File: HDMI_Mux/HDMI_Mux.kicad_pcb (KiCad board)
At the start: 2 copper layers, 12 parts, among them J1 505278-1933, J2 Conn_01x19_MountingPin, J3 Conn_01x19_MountingPin, U1 TS3DV20812, U2 ESD204DQAR-ES, U3 ESD204DQAR-ES, U4 ESD204DQAR-ES, U5 ESD204DQAR-ES

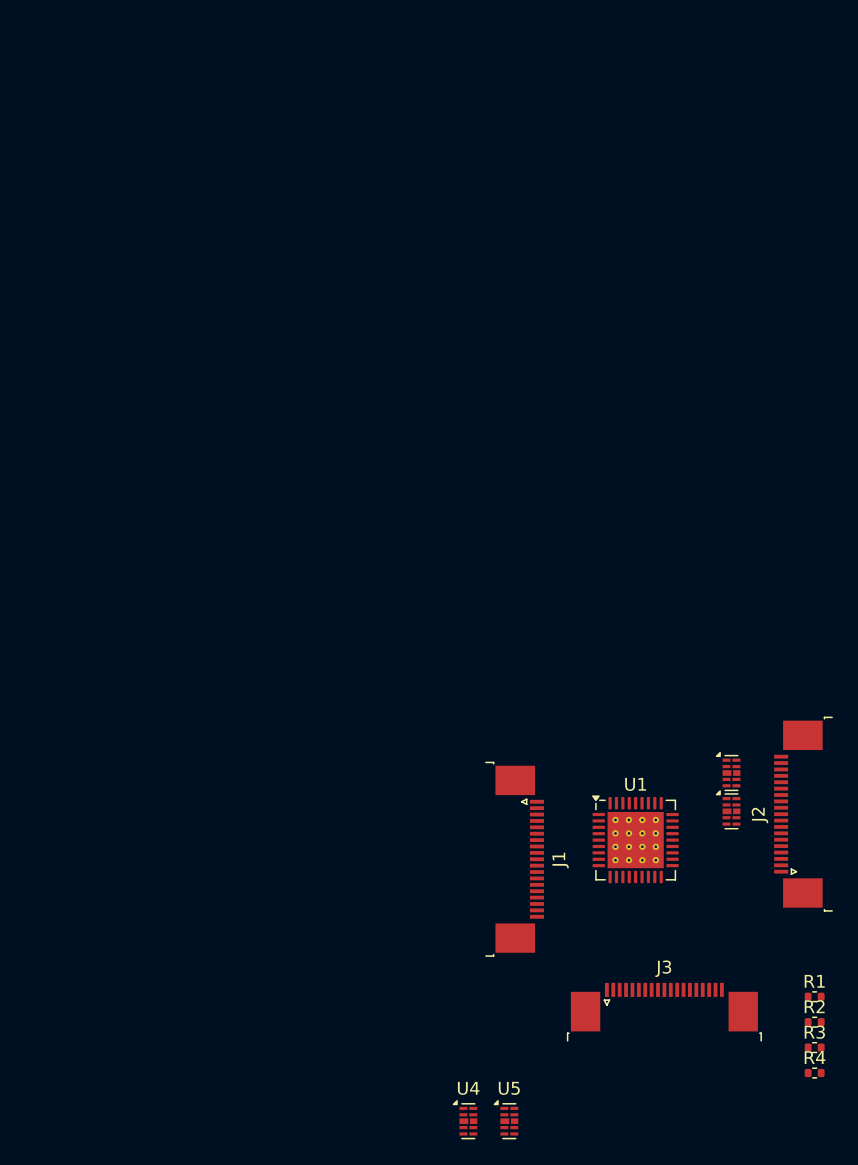
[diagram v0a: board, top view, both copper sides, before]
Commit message: Finish HDMI mux, misc improvements to cafebara
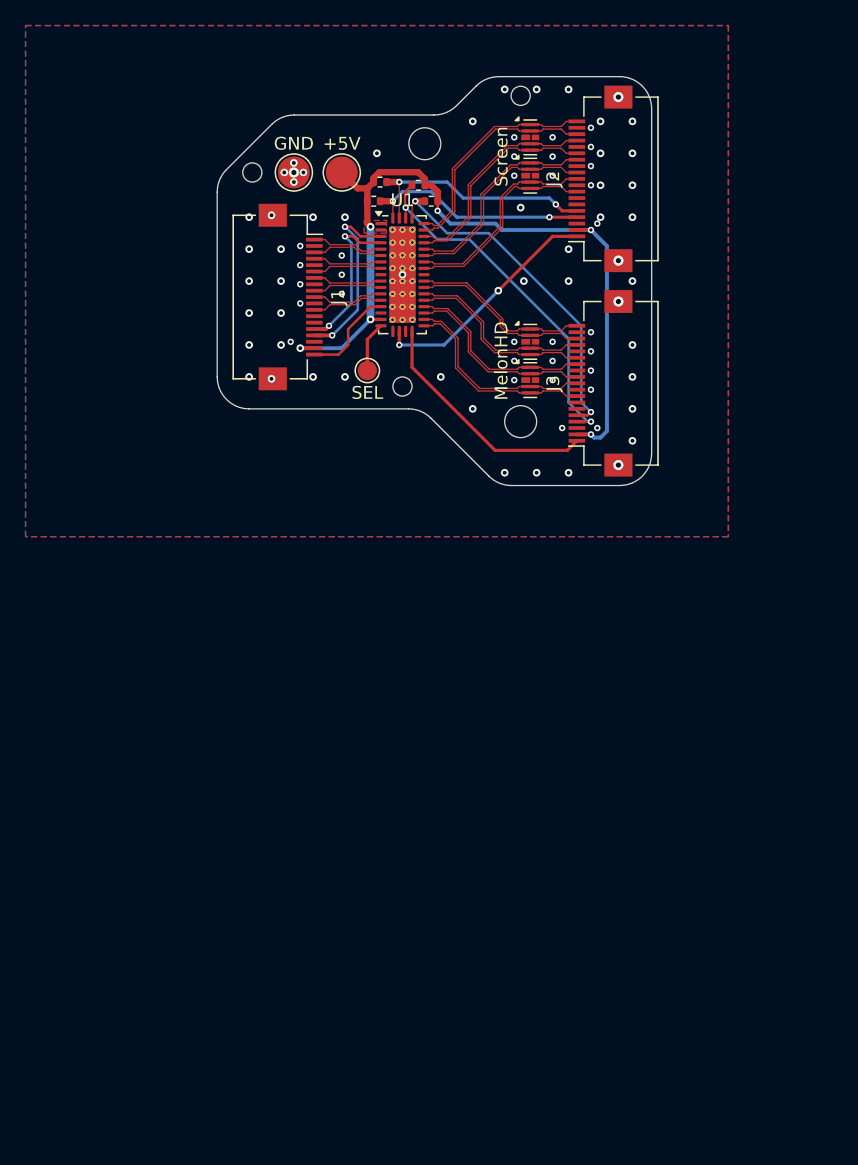
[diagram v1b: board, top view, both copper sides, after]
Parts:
- added TP1: +5V, TestPoint:TestPoint_Pad_D2.5mm, F.Cu at (94.8, 36.5)
- added TP2: GND, TestPoint:TestPoint_Pad_D2.5mm, F.Cu at (91.0, 36.5)
- added TP3: SEL, TestPoint:TestPoint_Pad_D1.5mm, F.Cu at (96.8, 52.0)
- J1, J2, J3: footprint Connector_FFC-FPC:TE_1-1734839-9_1x19-1MP_P0.5mm_Horizontal -> Connector_FFC-FPC:Hirose_FH12-19S-0.5SH_1x19-1MP_P0.50mm_Horizontal
- U1: value TS3DV20812 -> TS3DV642; footprint Package_DFN_QFN:Texas_RHH0036C_VQFN-36-1EP_6x6mm_P0.5mm_EP4.4x4.4mm_ThermalVias -> Package_DFN_QFN:WQFN-42-1EP_3.5x9mm_P0.5mm_EP2.05x7.55mm_ThermalVias
- moved R4 74.5 mm to (101.8, 38.8), turned to 180 degrees
- moved R3 74.3 mm to (100.8, 37.5), turned to 180 degrees
- moved R2 74.0 mm to (97.8, 37.2)
- moved R1 71.2 mm to (97.2, 38.8)
- moved U4 61.2 mm to (109.5, 49.8)
- moved U5 58.0 mm to (109.5, 52.8)
- moved U2 52.2 mm to (109.5, 33.8)
- moved U3 52.2 mm to (109.5, 36.8)
- moved J2 52.1 mm to (115.0, 37.0)
- moved J3 49.1 mm to (115.0, 53.0), turned to 90 degrees
- moved U1 47.9 mm to (99.5, 44.5)
- moved J1 47.5 mm to (90.8, 46.2)
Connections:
- U1 pad 1: TMDS2- -> +5V
- U1 pad 10: TMDSClk- -> TMDS0+
- U1 pad 11: GND -> TMDS0-
- U1 pad 12: /HDMI_SCL -> TMDSClk+
- U1 pad 13: SCL_A -> TMDSClk-
- U1 pad 14: SCL_B -> HPD
- U1 pad 15: TMDSClk_B- -> unconnected-(U1-CEC-Pad15)
- U1 pad 16: TMDSClk_B+ -> +5V
- U1 pad 17: TMDSClk_A- -> /SEL2
- U1 pad 18: TMDSClk_A+ -> unconnected-(U1-CEC_A-Pad18)
- U1 pad 19: TMDS0_B- -> HPD_A
- U1 pad 2: TMDS1+ -> +5V
- U1 pad 20: TMDS0_B+ -> unconnected-(U1-CEC_B-Pad20)
- U1 pad 21: TMDS0_A- -> HPD_B
- U1 pad 22: TMDS0_A+ -> TMDSClk_B-
- U1 pad 23: TMDS1_B- -> TMDSClk_B+
- U1 pad 24: TMDS1_B+ -> TMDS0_B-
- U1 pad 25: TMDS1_A- -> TMDS0_B+
- U1 pad 26: TMDS1_A+ -> TMDS1_B-
- U1 pad 27: SEL -> TMDS1_B+
- U1 pad 3: TMDS1- -> /HDMI_SDA
- U1 pad 30: TMDS2_A- -> unconnected-(U1-NC-Pad30)
- U1 pad 31: TMDS2_A+ -> TMDSClk_A-
- U1 pad 32: HPD_B -> TMDSClk_A+
- U1 pad 33: HPD_A -> TMDS0_A-
- U1 pad 34: HPD -> TMDS0_A+
- U1 pad 35: +3.3V -> TMDS1_A-
- U1 pad 36: TMDS2+ -> TMDS1_A+
- U1 pad 37: GND -> TMDS2_A-
- U1 pad 4: /HDMI_SDA -> /HDMI_SCL
- U1 pad 5: SDA_A -> TMDS2+
- U1 pad 6: SDA_B -> TMDS2-
- U1 pad 7: TMDS0+ -> TMDS1+
- U1 pad 8: TMDS0- -> TMDS1-
- U1 pad 9: TMDSClk+ -> unconnected-(U1-NC-Pad9)
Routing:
- net +5V: track 0.00 -> 62.5 mm, vias 0 -> 6
- net SDA_B: track 0.00 -> 28.3 mm, vias 0 -> 2
- net SCL_B: track 0.00 -> 27.5 mm, vias 0 -> 2
- net HPD_B: track 0.00 -> 18.7 mm
- net SCL_A: track 0.00 -> 18.6 mm, vias 0 -> 2
- net HPD_A: track 0.00 -> 18.5 mm, vias 0 -> 2
- net SDA_A: track 0.00 -> 17.9 mm, vias 0 -> 2
- net TMDS2_A+: track 0.00 -> 17.4 mm
- net TMDS2_A-: track 0.00 -> 17.4 mm
- net TMDS1_A+: track 0.00 -> 16.8 mm
- net TMDS1_A-: track 0.00 -> 16.8 mm
- net TMDS0_A-: track 0.00 -> 16.4 mm
- net TMDS0_A+: track 0.00 -> 16.4 mm
- net TMDSClk_A-: track 0.00 -> 16.2 mm
- net TMDSClk_A+: track 0.00 -> 16.2 mm
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- added copper zone on F.Cu, net +5V
- added copper zone on B.Cu, net GND
- added copper zone on F.Cu, net GND
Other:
- board outline added: 34 x 32 mm
- board text added: "MelonHD"
- board text added: "Screen"

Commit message: Misc improvements to several boards
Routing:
- net GND: vias 84 -> 81
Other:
- outline, holes or cut-outs redrawn

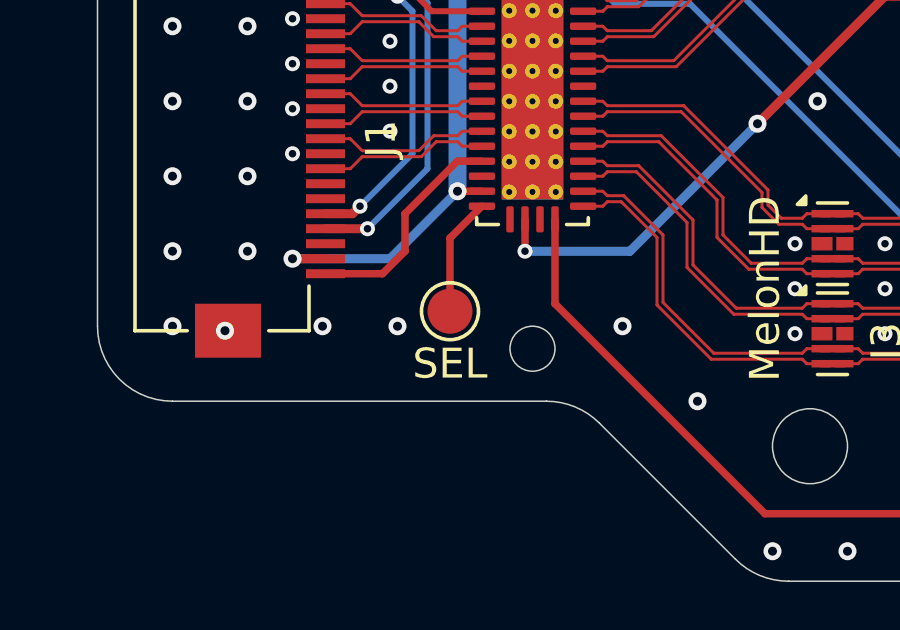
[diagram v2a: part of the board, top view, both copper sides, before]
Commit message: Move to using 100W-Charging-PCB for battery charge
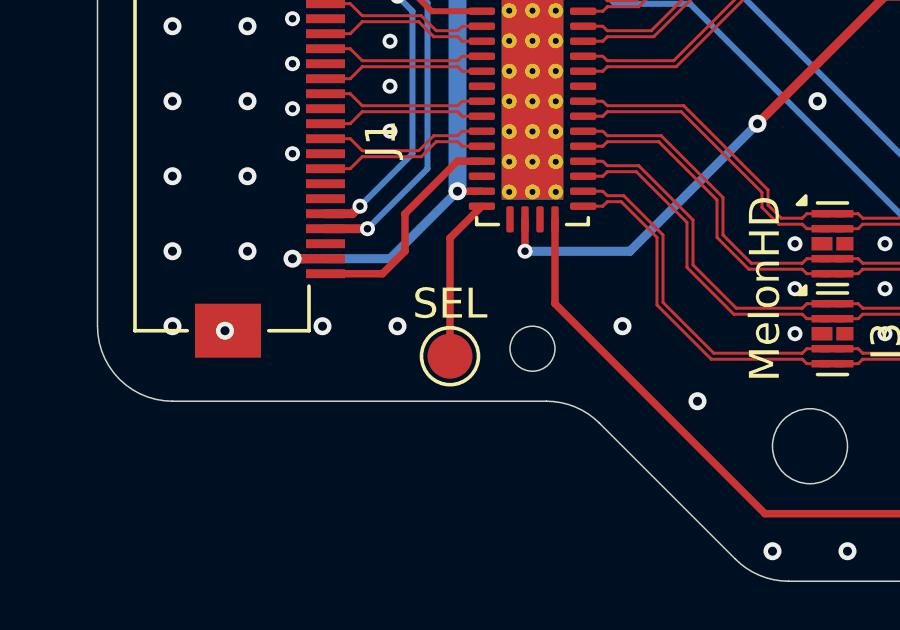
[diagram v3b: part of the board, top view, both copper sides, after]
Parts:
- moved TP3 1.50 mm to (96.8, 53.5), turned to 180 degrees
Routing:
- net /SEL2: track 3.94 -> 5.44 mm
